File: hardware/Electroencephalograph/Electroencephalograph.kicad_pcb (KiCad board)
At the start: 2 copper layers, 90 x 85 mm, 263 parts, among them J1 Conn_01x08_Male, J2 Conn_01x08_Male, U1 ADS1298IPAG, U10 TPS60403, U2 OPA330xxD, U3 DSPIC33FJ128MC710A, U4 THI3-0511, U5 ADUM2401BRWZ, U7 LP5912-1.8DRVT, U8 LP5912-1.8DRVT, U9 LP5912-1.8DRVT

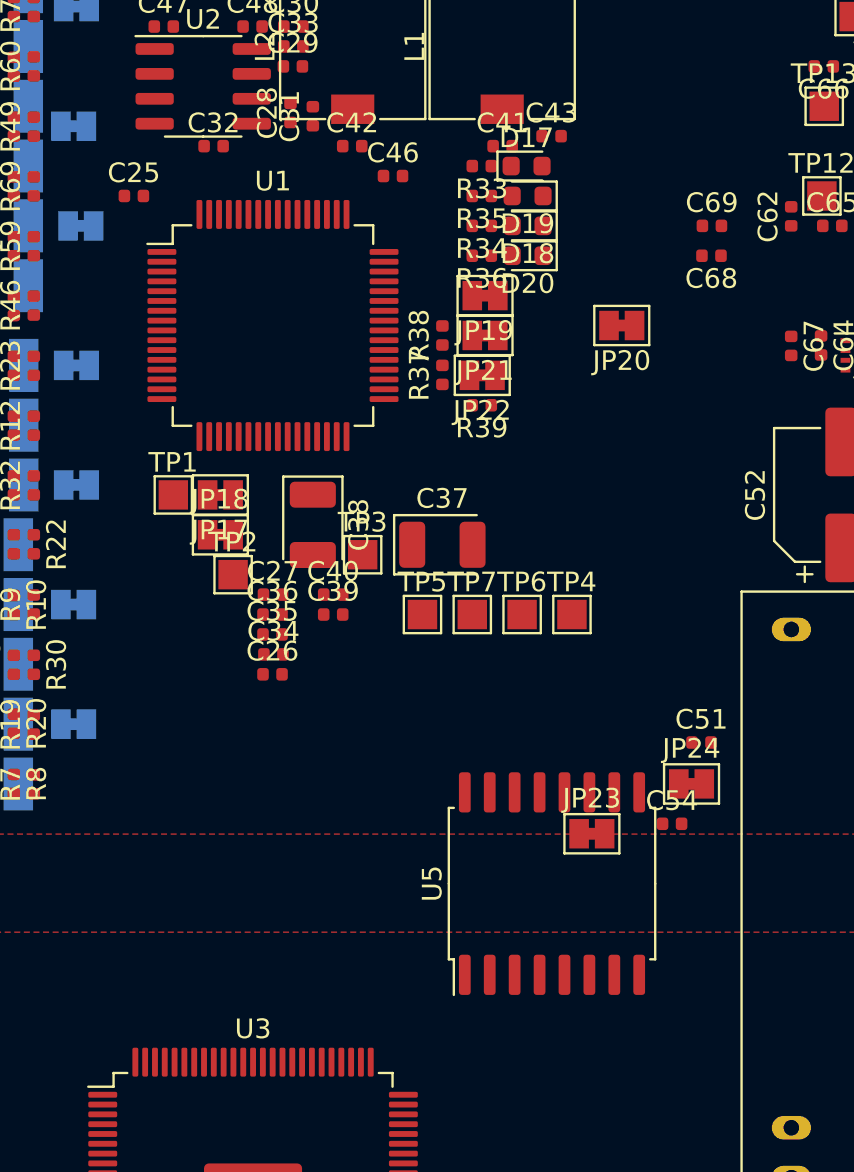
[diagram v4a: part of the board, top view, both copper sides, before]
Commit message: fixed spi lines
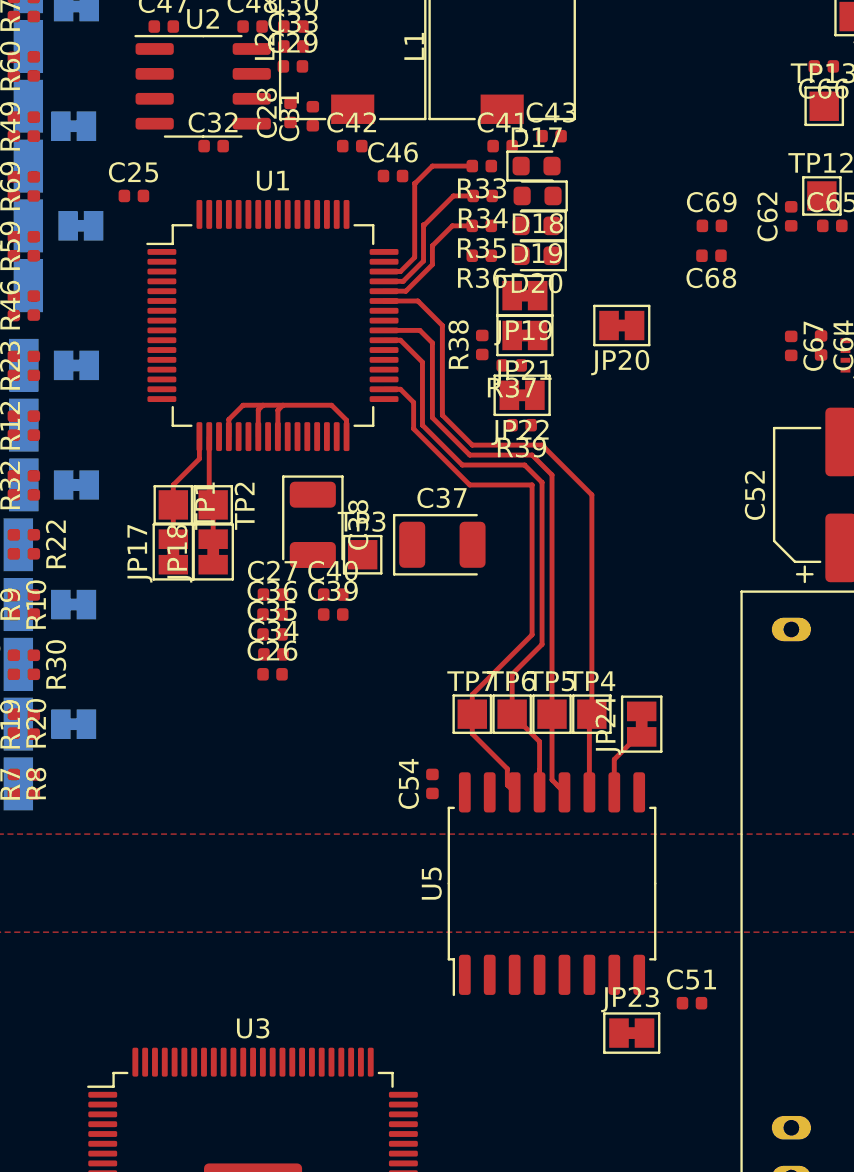
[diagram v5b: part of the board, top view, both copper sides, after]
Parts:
- moved C51 13.3 mm to (116.4, 71.1)
- moved C54 12.4 mm to (103.1, 59.9), turned to 90 degrees
- moved JP23 10.4 mm to (113.3, 72.6)
- moved TP5 8.33 mm to (109.2, 56.4)
- moved TP4 5.18 mm to (111.3, 56.4)
- moved TP6 5.11 mm to (107.2, 56.4)
- moved TP7 5.08 mm to (105.2, 56.4)
- moved JP24 3.97 mm to (113.8, 56.9), turned to 90 degrees
- moved JP17 3.77 mm to (89.9, 48.1), turned to 90 degrees
- moved TP2 3.70 mm to (91.9, 45.7), turned to 270 degrees
- moved R37 3.57 mm to (107.2, 38.6), turned to 180 degrees
- moved JP22 2.27 mm to (107.7, 40.1)
- moved R39 2.27 mm to (107.7, 41.7)
- moved R38 2.09 mm to (105.7, 37.6)
- moved JP19 2.03 mm to (107.8, 35.1)
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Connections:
- JP18 pad 1: (no net) -> A_VDD
- U5 pad 12: EEG_CS -> EEG_SCK
- U5 pad 13: EEG_MOSI -> EEG_CS
- U5 pad 14: EEG_SCK -> EEG_MOSI
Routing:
- net EEG_MISO: track 0.00 -> 32.6 mm
- net EEG_CS: track 0.00 -> 31.1 mm
- net EEG_SCK: track 0.00 -> 30.8 mm
- net EEG_MOSI: track 0.00 -> 28.2 mm
- net A_VSS: track 0.00 -> 11.7 mm
- net Net-(R33-Pad2): track 0.00 -> 8.94 mm
- net Net-(R34-Pad2): track 0.00 -> 7.43 mm
- net Net-(R35-Pad2): track 0.00 -> 6.44 mm
- net Net-(JP17-Pad2): track 0.00 -> 5.78 mm
- net Net-(JP18-Pad2): track 0.00 -> 5.31 mm
- net Net-(JP24-Pad1): track 0.00 -> 3.55 mm

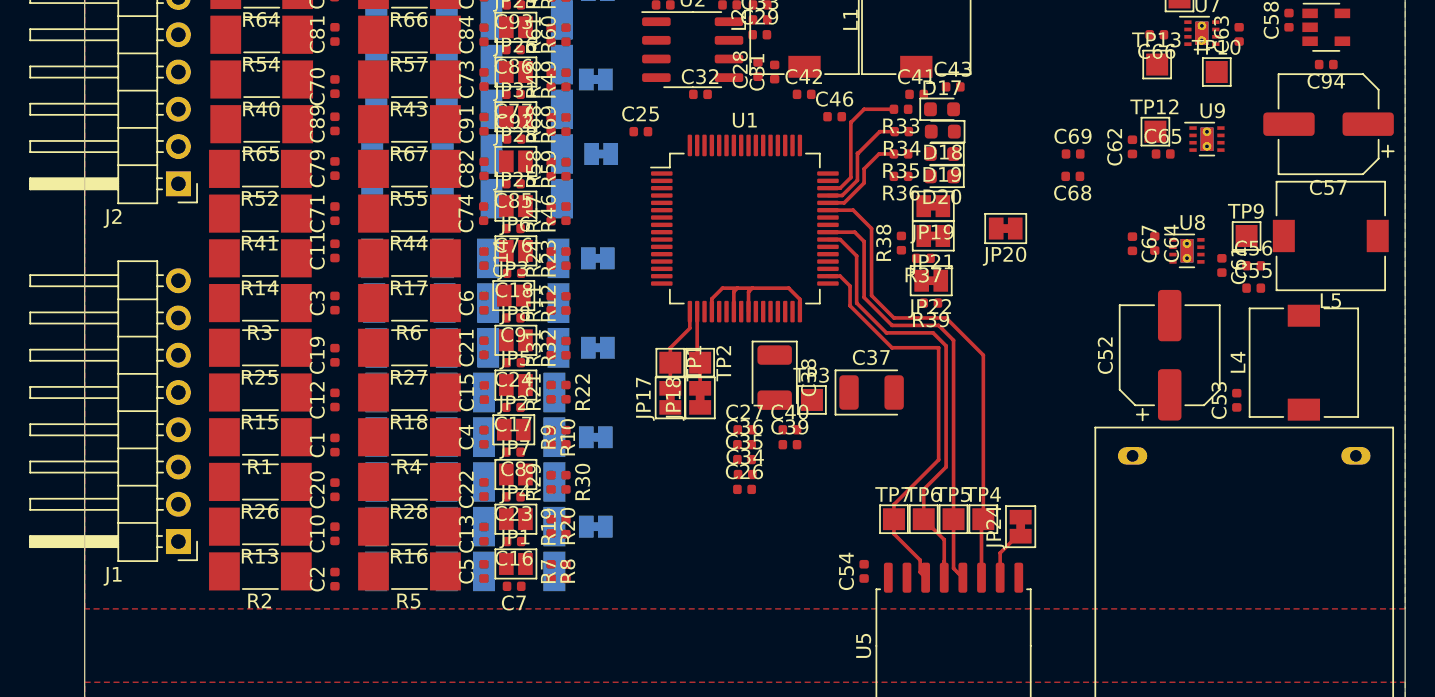
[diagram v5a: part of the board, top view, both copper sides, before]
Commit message: split of analog and digital ground
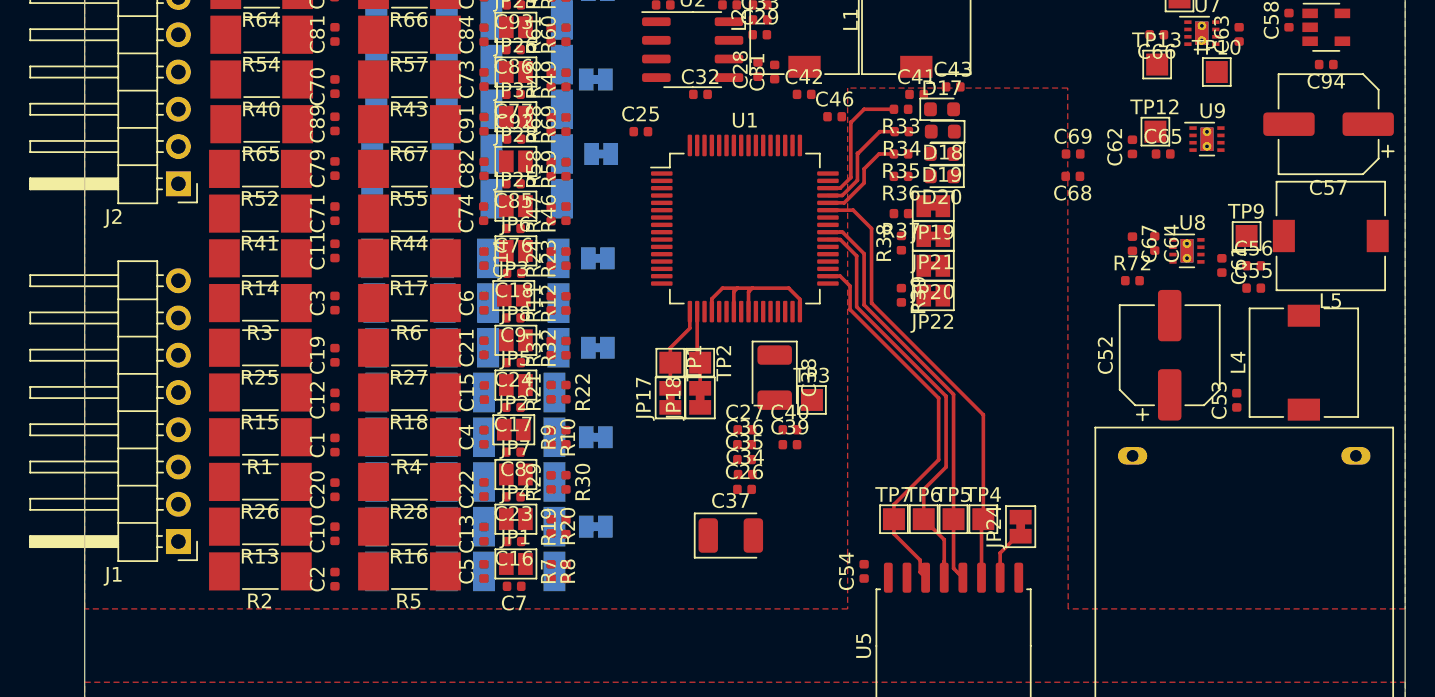
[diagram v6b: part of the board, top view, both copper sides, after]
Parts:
- added R72: 0R, Resistor_SMD:R_0402_1005Metric, F.Cu at (121.4, 40.1)
- moved C37 13.7 mm to (94.0, 57.5)
- moved JP20 5.55 mm to (107.8, 39.1)
- moved R37 3.41 mm to (105.6, 35.6)
- moved R39 2.08 mm to (105.7, 41.1), turned to 270 degrees
- moved JP22 1.03 mm to (107.8, 41.1)
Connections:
- C43 pad 2: A_GND -> D_GND
- C46 pad 2: A_GND -> D_GND
- C54 pad 2: A_GND -> D_GND
- C61 pad 2: A_GND -> D_GND
- C64 pad 2: A_GND -> D_GND
- C67 pad 2: A_GND -> D_GND
- D17 pad 1: A_GND -> D_GND
- D18 pad 1: A_GND -> D_GND
- D19 pad 1: A_GND -> D_GND
- D20 pad 1: A_GND -> D_GND
- JP19 pad 1: A_GND -> D_GND
- R37 pad 1: A_GND -> D_GND
- R38 pad 1: A_GND -> D_GND
- R39 pad 1: A_GND -> D_GND
- U1 pad 33: A_GND -> D_GND
- U1 pad 49: A_GND -> D_GND
- U1 pad 51: A_GND -> D_GND
- U1 pad 52: A_GND -> D_GND
- U5 pad 15: A_GND -> D_GND
- U5 pad 9: A_GND -> D_GND
- U8 pad 3: A_GND -> D_GND
- U8 pad 5: A_GND -> D_GND
- U8 pad 7: A_GND -> D_GND
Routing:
- net EEG_SCK: track 30.8 -> 28.5 mm
- net EEG_MISO: track 32.6 -> 30.5 mm
- net EEG_CS: track 31.1 -> 29.2 mm
- net EEG_MOSI: track 28.2 -> 26.3 mm

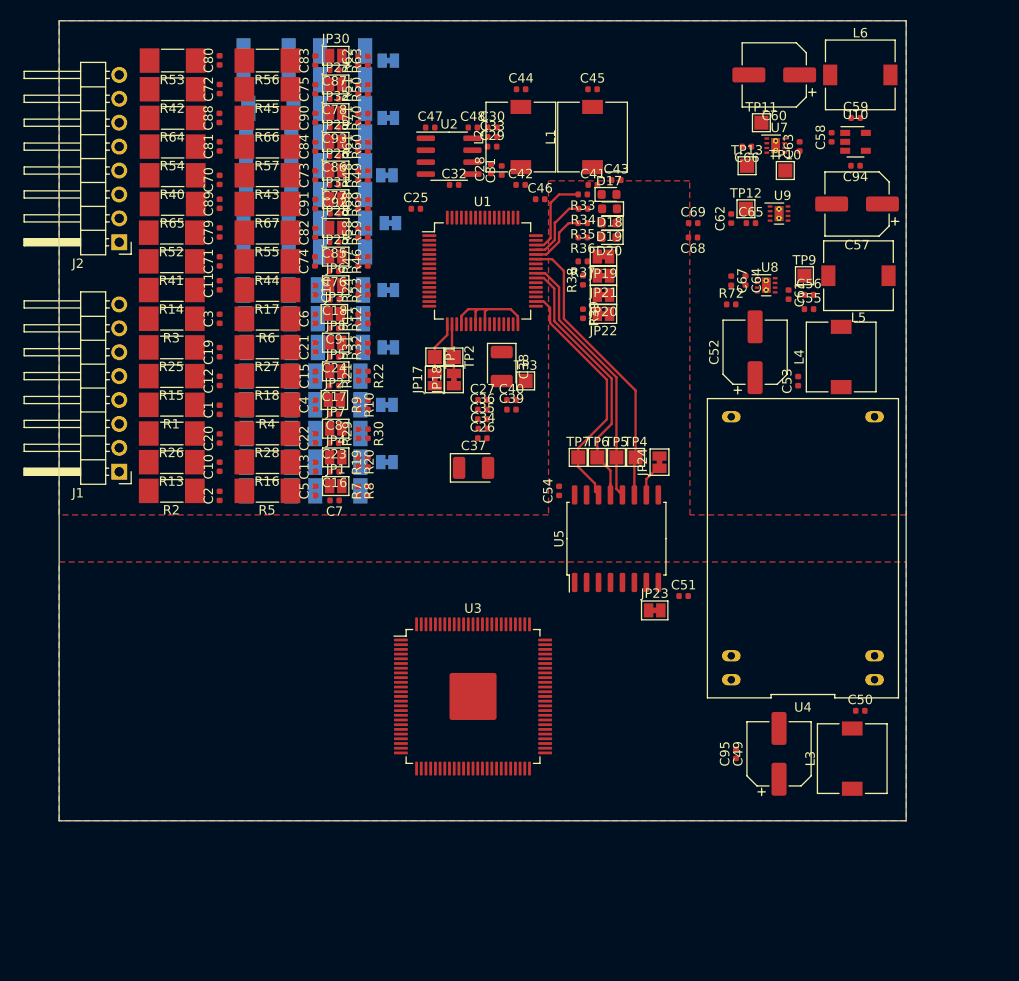
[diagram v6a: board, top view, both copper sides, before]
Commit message: added procesing unit
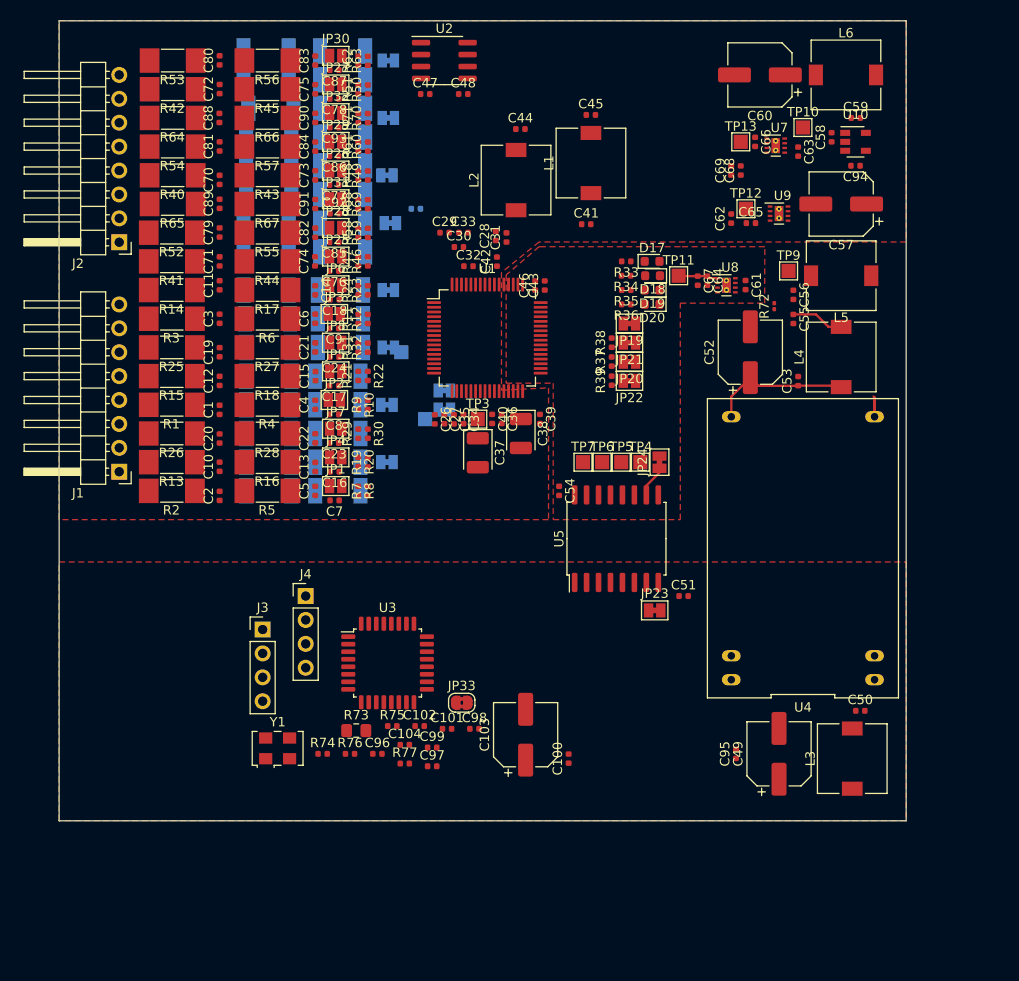
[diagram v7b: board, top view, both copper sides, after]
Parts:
- added C100: 100n, Capacitor_SMD:C_0402_1005Metric, F.Cu at (104.1, 88.4)
- added C101: 100n, Capacitor_SMD:C_0402_1005Metric, F.Cu at (91.2, 85.2)
- added C102: 100n, Capacitor_SMD:C_0402_1005Metric, F.Cu at (88.3, 84.9)
- added C103: 220u, Capacitor_SMD:CP_Elec_6.3x5.8, F.Cu at (99.6, 85.9)
- added C104: 100n, Capacitor_SMD:C_0402_1005Metric, F.Cu at (86.7, 86.9)
- added C96: 8p, Capacitor_SMD:C_0402_1005Metric, F.Cu at (83.8, 87.9)
- added C97: 8p, Capacitor_SMD:C_0402_1005Metric, F.Cu at (89.6, 89.2)
- added C98: 100n, Capacitor_SMD:C_0402_1005Metric, F.Cu at (94.1, 85.2)
- added C99: 100n, Capacitor_SMD:C_0402_1005Metric, F.Cu at (89.6, 87.2)
- added J3: Conn_01x04_Female, Connector_PinHeader_2.54mm:PinHeader_1x04_P2.54mm_Vertical, F.Cu at (71.6, 74.7)
- added J4: Conn_01x04_Female, Connector_PinHeader_2.54mm:PinHeader_1x04_P2.54mm_Vertical, F.Cu at (76.2, 71.1)
- added JP33: Jumper_NC_Small, Jumper:SolderJumper-2_P1.3mm_Bridged2Bar_RoundedPad1.0x1.5mm, F.Cu at (92.8, 82.5)
- added R73: 2k2, Resistor_SMD:R_0805_2012Metric_Pad1.15x1.40mm_HandSolder, F.Cu at (81.6, 85.4)
- added R74: 2k2, Resistor_SMD:R_0402_1005Metric, F.Cu at (78.0, 87.9)
- added R75: 10k, Resistor_SMD:R_0402_1005Metric, F.Cu at (85.4, 84.9)
- added R76: 220R, Resistor_SMD:R_0402_1005Metric, F.Cu at (80.9, 87.9)
- added R77: 220R, Resistor_SMD:R_0402_1005Metric, F.Cu at (86.7, 88.9)
- added Y1: 20MHz, Oscillator:Oscillator_SMD_EuroQuartz_XO53-4Pin_5.0x3.2mm, F.Cu at (73.2, 87.3)
- C25, JP17, JP18, TP1, TP2: moved to B.Cu
- R72: footprint Resistor_SMD:R_0402_1005Metric -> Resistor_SMD:R_0201_0603Metric
- U3: value DSPIC33FJ128MC710A -> STM32F030K6Tx; footprint Package_QFP:TQFP-100-1EP_14x14mm_P0.5mm_EP5x5mm -> Package_QFP:LQFP-32_7x7mm_P0.8mm
- moved TP11 18.5 mm to (115.8, 37.1)
- moved C43 13.5 mm to (101.6, 38.1), turned to 90 degrees
- moved C30 13.2 mm to (92.5, 34.0)
- moved R37 11.1 mm to (108.7, 46.2), turned to 90 degrees
- moved C33 10.6 mm to (93.0, 32.5)
- moved C29 10.4 mm to (91.0, 32.5)
- moved U2 10.2 mm to (90.9, 14.2)
- moved U3 9.75 mm to (84.9, 78.2)
- moved C46 9.18 mm to (100.6, 38.1), turned to 90 degrees
- moved C32 8.77 mm to (93.5, 36.1)
- moved C68 8.74 mm to (122.4, 25.9), turned to 90 degrees
- moved C42 8.53 mm to (96.5, 35.6), turned to 90 degrees
- moved R33 8.48 mm to (110.3, 35.6)
- moved R35 8.48 mm to (110.3, 38.6)
- moved R36 8.48 mm to (110.3, 40.1)
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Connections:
- U3 pad 1: (no net) -> 5V_DIGITAL
- U3 pad 15: VSS -> (no net)
- U3 pad 16: (no net) -> GND
- U3 pad 17: (no net) -> 5V_DIGITAL
- U3 pad 19: (no net) -> SCL
- U3 pad 2: (no net) -> Net-(C96-Pad2)
- U3 pad 20: (no net) -> SDA
- U3 pad 23: (no net) -> /EEGDataProcessing/SWDIO
- U3 pad 24: (no net) -> /EEGDataProcessing/SWCLK
- U3 pad 29: (no net) -> /EEGDataProcessing/USART_TX
- U3 pad 3: (no net) -> Net-(C97-Pad2)
- U3 pad 30: (no net) -> /EEGDataProcessing/USART_RX
- U3 pad 31: (no net) -> Net-(JP33-Pad2)
- U3 pad 32: (no net) -> GND
- U3 pad 4: (no net) -> /EEGDataProcessing/NRST
- U3 pad 5: (no net) -> 5V_DIGITAL
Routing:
- net EEG_MISO: track 30.5 -> 0.00 mm
- net EEG_CS: track 29.2 -> 0.00 mm
- net EEG_SCK: track 28.5 -> 0.00 mm
- net EEG_MOSI: track 26.3 -> 0.00 mm
- net Net-(C52-Pad1): track 0.00 -> 15.1 mm
- net A_VSS: track 11.7 -> 0.00 mm
- net Net-(R33-Pad2): track 8.94 -> 0.00 mm
- net Net-(R34-Pad2): track 7.43 -> 0.00 mm
- net Net-(R35-Pad2): track 6.44 -> 0.00 mm
- net Net-(JP17-Pad2): track 5.78 -> 0.00 mm
- net ECC_POWER_SUPPLY: track 0.00 -> 5.63 mm
- net Net-(JP18-Pad2): track 5.31 -> 0.00 mm
- net A_GND: track 0.00 -> 4.25 mm
- net D_VDD: track 0.00 -> 4.24 mm
- added copper zone on F.Cu, net D_GND

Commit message: eeg digital part routing
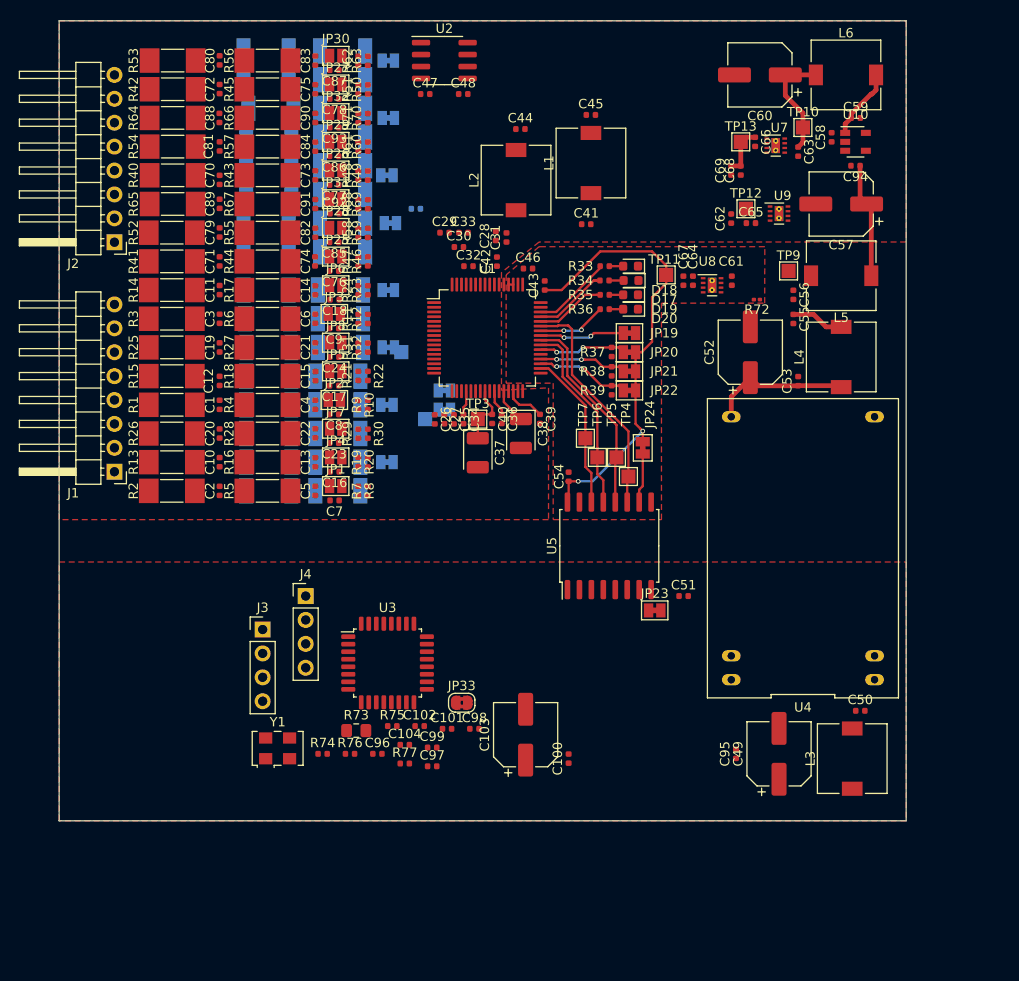
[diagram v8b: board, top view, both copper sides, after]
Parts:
- moved JP21 3.05 mm to (110.6, 47.2)
- moved R38 3.05 mm to (108.7, 47.2)
- moved TP7 2.55 mm to (105.9, 54.4)
- moved JP24 2.34 mm to (112.0, 55.4)
- moved R35 2.34 mm to (108.0, 39.1)
- moved R36 2.34 mm to (108.0, 40.6)
- moved D18 2.34 mm to (110.8, 37.6)
- moved R33 2.34 mm to (108.0, 36.1)
- moved R34 2.34 mm to (108.0, 37.6)
- moved D19 2.34 mm to (110.7, 39.1)
- moved D20 2.34 mm to (110.7, 40.6)
- moved D17 2.34 mm to (110.7, 36.1), turned to 180 degrees
- moved TP4 1.98 mm to (110.5, 58.4)
- moved R72 1.97 mm to (124.1, 39.6), turned to 180 degrees
- moved C46 1.96 mm to (99.8, 36.3), turned to 0 degrees
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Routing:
- net D_VDD: track 4.24 -> 48.8 mm, vias 0 -> 2
- net EEG_MISO: track 0.00 -> 23.8 mm
- net EEG_SCK: track 0.00 -> 21.7 mm
- net EEG_CS: track 0.00 -> 20.7 mm
- net EEG_MOSI: track 0.00 -> 16.7 mm
- net Net-(C57-Pad1): track 0.00 -> 12.2 mm
- net Net-(C60-Pad1): track 0.00 -> 11.9 mm
- net Net-(JP22-Pad2): track 0.00 -> 9.96 mm, vias 0 -> 2
- net Net-(JP21-Pad2): track 0.00 -> 9.33 mm, vias 0 -> 2
- net Net-(JP20-Pad2): track 0.00 -> 9.32 mm, vias 0 -> 2
- net Net-(JP19-Pad2): track 0.00 -> 9.08 mm, vias 0 -> 2
- net Net-(R33-Pad2): track 0.00 -> 8.45 mm
- net A_VSS: track 0.00 -> 7.91 mm
- net Net-(R34-Pad2): track 0.00 -> 7.89 mm
- net Net-(C59-Pad1): track 0.00 -> 7.58 mm
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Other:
- net class Default: clearance 0.2 -> 0.1778; via_dia 0.8 -> 0.5; via_drill 0.4 -> 0.3
- rule pad_to_mask_clearance: 0.051 -> 0.05
- rule trace_clearance: 0.2 -> 0.1778
